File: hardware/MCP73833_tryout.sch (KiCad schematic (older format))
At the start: 14 parts, among them J1 LOAD, J2 BAT, U1 MCP73833, U2 USB_Micro

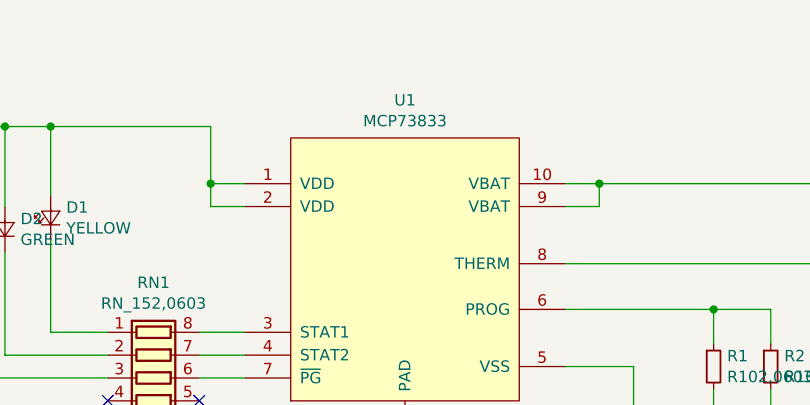
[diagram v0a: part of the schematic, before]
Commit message: update for MCP73833 DFN,
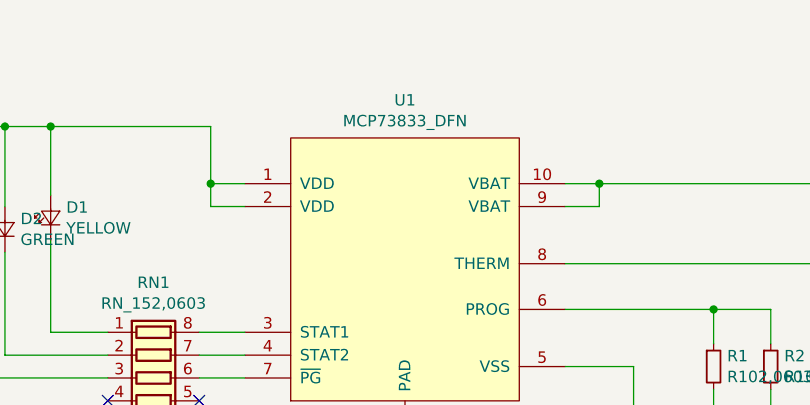
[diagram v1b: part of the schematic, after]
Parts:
- removed U1: MCP73833, footprint-lib:MCP73833, symbol taobao-components:MCP73833
- added U1: MCP73833_DFN, footprint-lib:MCP73833_DFN, symbol taobao-components:MCP73833_DFN
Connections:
- net +5V: now also U1.1 (VDD), U1.2 (VDD)
- net GND: now also U1.11 (PAD), U1.5 (VSS)
- net at C2.1, J1.1 (Pin_1), J2.1 (Pin_1): now also U1.10 (VBAT), U1.9 (VBAT)
- net at RN1.8 (R1.2): now also U1.3 (STAT1)
- net at RN1.7 (R2.2): now also U1.4 (STAT2)
- net at R1.1, R2.1: now also U1.6 (PROG)
- net at RN1.6 (R3.2): now also U1.7 (~PG~)
- net at R3.1, TH1.1: now also U1.8 (THERM)
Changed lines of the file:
@@
 EESchema Schematic File Version 4
+LIBS:MCP73833_tryout-cache
 EELAYER 29 0
 EELAYER END
@@
 Comment4 ""
 $EndDescr
-$Comp
-L taobao-components:MCP73833 U1
-U 1 1 5D03B616
-P 3750 2350
-F 0 "U1" H 3750 3115 50  0000 C CNN
-F 1 "MCP73833" H 3750 3024 50  0000 C CNN
-F 2 "footprint-lib:MCP73833" H 3750 1500 50  0001 C CNN
-F 3 "" H 3750 1500 50  0001 C CNN
-	1    3750 2350
-	1    0    0    -1
-$EndComp
 $Comp
 L power:+5V #PWR0101
@@
 Wire Wire Line
 	4750 3250 4750 3600
+$Comp
+L taobao-components:MCP73833_DFN U1
+U 1 1 5D0406D8
+P 3750 2350
+F 0 "U1" H 3750 3115 50  0000 C CNN
+F 1 "MCP73833_DFN" H 3750 3024 50  0000 C CNN
+F 2 "footprint-lib:MCP73833_DFN" H 3750 1150 50  0001 C CNN
+F 3 "" H 3750 1150 50  0001 C CNN
+	1    3750 2350
+	1    0    0    -1
+$EndComp
 $EndSCHEMATC
